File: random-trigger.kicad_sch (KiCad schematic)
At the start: 69 parts, among them J1 Eurorack Power, J10 Trigger Out B, J11 Inv Trigger Out B, J2 Noise In, J3 Noise Out, J4 Trigger In A, J5 Gate Out A, J6 Trigger Out A, J7 Inv Trigger Out A, J8 Trigger In B, J9 Gate Out B, Q1 2N3904, Q2 2N3904, U1 TL074, U2 LM7805_TO220, U3 4013, U4 4081

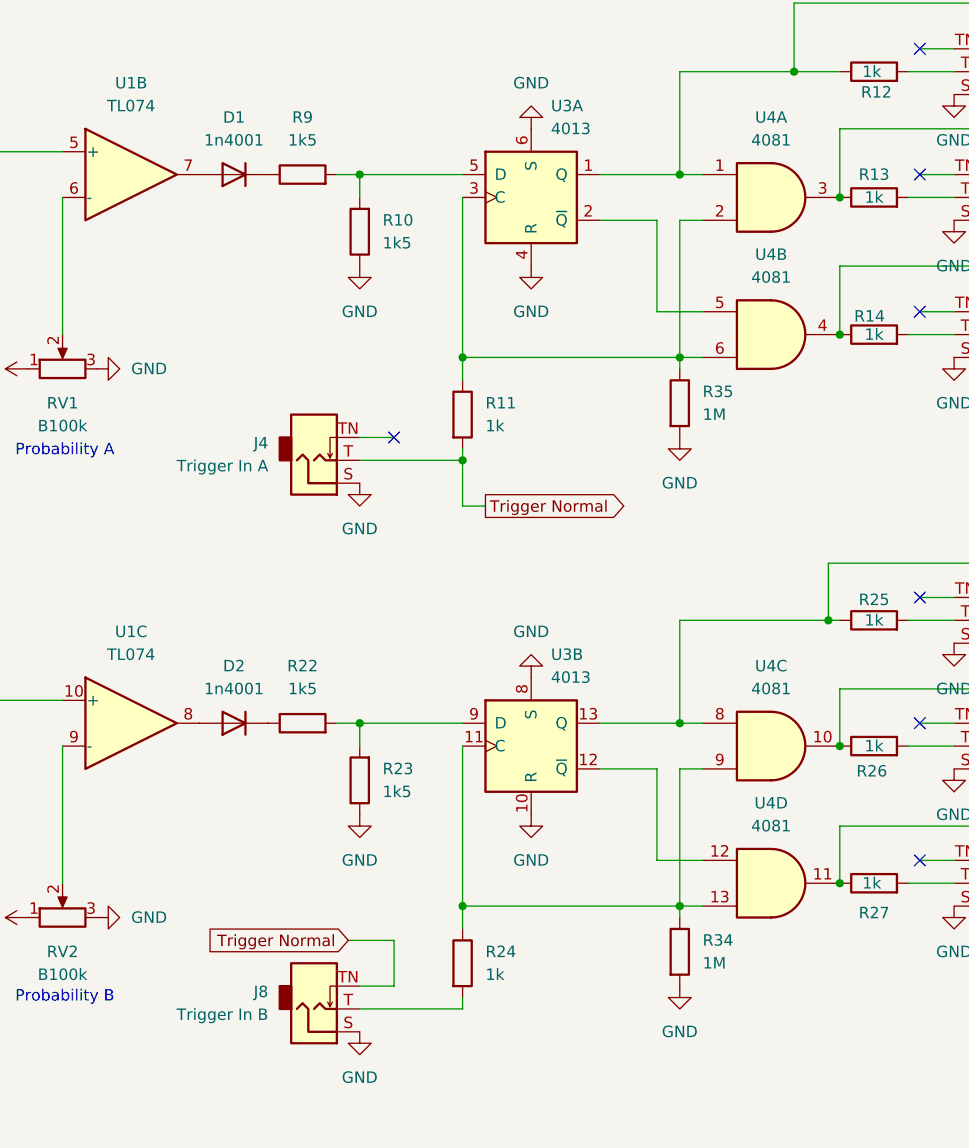
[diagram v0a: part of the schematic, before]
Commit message: Add trigger normalling and switch to using kicad-libraries
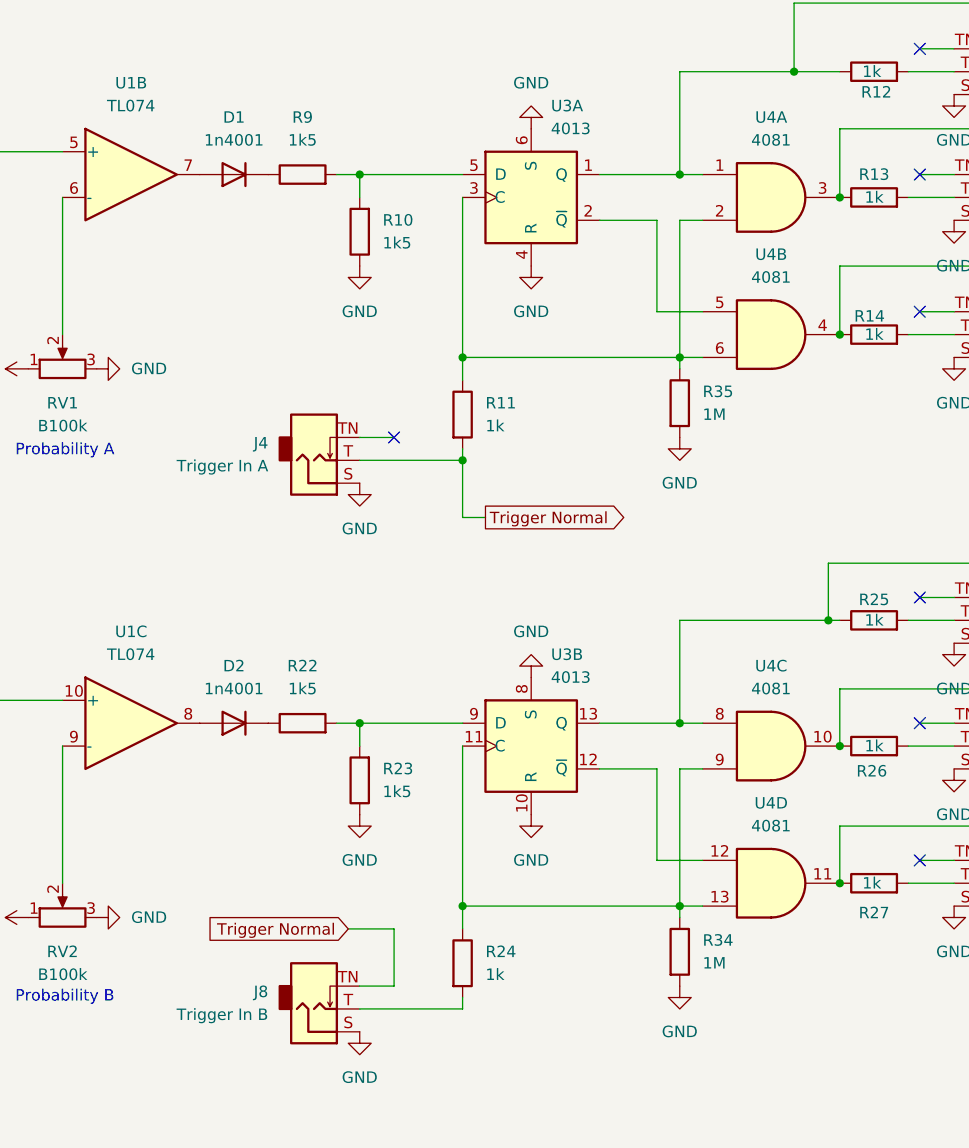
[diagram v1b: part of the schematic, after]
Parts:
- J10, J11, J2, J3, J4, J5, J6, J7, J8, J9: footprint Extras:Jack_3.5mm_QingPu_WQP-PJ301BM_Vertical -> MAI_Connector_Audio:Jack_3.5mm_QingPu_WQP-PJ301BM_Vertical
- RV1, RV2: footprint Potentiometer_THT:Potentiometer_Alpha_RD901F-40-00D_Single_Vertical -> MAI_Potentiometer_THT:Potentiometer_Alpha_RD901F-40-00D_Single_Vertical

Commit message: Redo PCB to have all components on front
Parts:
- removed J2: Noise In, MAI_Connector_Audio:Jack_3.5mm_QingPu_WQP-PJ301BM_Vertical, symbol Connector:AudioJack2_SwitchT
- removed R5: 1k, Resistor_THT:R_Axial_DIN0207_L6.3mm_D2.5mm_P7.62mm_Horizontal, symbol Device:R
- removed unit 3 of U1
- removed unit 1 of U1
- removed unit 4 of U1
- removed unit 2 of U1
- added unit 1 of U2
- added unit 3 of U2
- added unit 4 of U2
- added unit 2 of U2
- C1: renamed from C2; footprint Capacitor_THT:CP_Radial_D6.3mm_P2.50mm -> Capacitor_THT:CP_Radial_D5.0mm_P2.50mm
- C2: renamed from C1; footprint Capacitor_THT:CP_Radial_D6.3mm_P2.50mm -> Capacitor_THT:CP_Radial_D5.0mm_P2.50mm
- U1: renamed from U2; value LM7805_TO220 -> L78L05_TO92; footprint Package_TO_SOT_THT:TO-220-3_Vertical -> Package_TO_SOT_THT:TO-92_Inline; symbol Regulator_Linear:LM7805_TO220 -> Regulator_Linear:L78L05_TO92
- U2: renamed from U1; footprint Package_DIP:DIP-14_W7.62mm_Socket -> MAI_Package_DIP:DIP-14_W7.62mm_Socket_WithChip
- U3, U4: footprint Package_DIP:DIP-14_W7.62mm_Socket -> MAI_Package_DIP:DIP-14_W7.62mm_Socket_WithChip
- renumbered D3 to D2, D4 to D3, D5 to D4, D2 to D5, J11 to J10, J4 to J2, J5 to J3, J6 to J4, J7 to J5, J3 to J6, J8 to J7, J9 to J8, J10 to J9, R11 to R10, R35 to R11, R28 to R15, R29 to R16, R30 to R17, R15 to R18, R16 to R19, R17 to R20, R18 to R21, R19 to R22, R20 to R23, R21 to R24, R22 to R25, R23 to R26, R24 to R27, R34 to R28, R25 to R29, R26 to R30, R27 to R31, R31 to R32, R32 to R33, R33 to R34, R6 to R5, R7 to R6, R8 to R7, R9 to R8, R10 to R9
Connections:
- net +12V: now also U1.3 (VI); no longer U1.1 (VI)
- net +5V: now also U1.1 (VO); no longer U1.3 (VO)
- net at U3.12 (~{Q}): now also U4.8; no longer U4.12
- net at D6.2 (A), R29.1, U3.13 (Q): now also U4.12; no longer U4.8
- net at D5.2 (A): now also U2.7
- net at C5.1: now also R4.2, R5.1, U2.14
- net at R3.1, R4.1: now also U2.13 (-)
- net at C7.2, R23.2, R24.1: now also U2.5 (+)
- net at RV2.2: now also U2.6 (-)
- net at D8.2 (A), R31.1: now also U4.10; no longer U4.11
- net at C5.2, R6.2, R7.1: now also U2.3 (+)
- net at C4.2, R2.1: now also U2.12 (+)
- net at R21.2, R22.1: now also U2.8
- net at C6.2, R19.1: now also U2.10 (+)
- net at R20.1, R21.1: now also U2.9 (-)
- net at RV1.2: now also U2.2 (-)
- net at D1.2 (A): now also U2.1
- net at D7.2 (A), R30.1: now also U4.11; no longer U4.10

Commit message: Use correct box capacitor footprint
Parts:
- C4, C5, C6, C7: footprint Capacitor_THT:C_Rect_L7.0mm_W3.5mm_P5.00mm -> Capacitor_THT:C_Rect_L7.2mm_W3.5mm_P5.00mm_FKS2_FKP2_MKS2_MKP2
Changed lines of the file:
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@@
 			)
 		)
-		(property "Footprint" "Capacitor_THT:C_Rect_L7.0mm_W3.5mm_P5.00mm"
+		(property "Footprint" "Capacitor_THT:C_Rect_L7.2mm_W3.5mm_P5.00mm_FKS2_FKP2_MKS2_MKP2"
 			(at 53.34 96.8248 0)
 			(effects
@@
 			)
 		)
-		(property "Footprint" "Capacitor_THT:C_Rect_L7.0mm_W3.5mm_P5.00mm"
+		(property "Footprint" "Capacitor_THT:C_Rect_L7.2mm_W3.5mm_P5.00mm_FKS2_FKP2_MKS2_MKP2"
 			(at 115.57 35.8648 0)
 			(effects
@@
 			)
 		)
-		(property "Footprint" "Capacitor_THT:C_Rect_L7.0mm_W3.5mm_P5.00mm"
+		(property "Footprint" "Capacitor_THT:C_Rect_L7.2mm_W3.5mm_P5.00mm_FKS2_FKP2_MKS2_MKP2"
 			(at 53.34 35.8648 0)
 			(effects
@@
 			)
 		)
-		(property "Footprint" "Capacitor_THT:C_Rect_L7.0mm_W3.5mm_P5.00mm"
+		(property "Footprint" "Capacitor_THT:C_Rect_L7.2mm_W3.5mm_P5.00mm_FKS2_FKP2_MKS2_MKP2"
 			(at 115.57 96.8248 0)
 			(effects
